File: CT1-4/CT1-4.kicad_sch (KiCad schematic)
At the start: 25 parts

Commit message: Some initial fixing of ERC errors.
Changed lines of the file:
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@@
 	)
 	(junction
-		(at 57.15 33.02)
-		(diameter 0)
-		(color 0 0 0 0)
-	)
-	(junction
 		(at 204.47 327.66)
 		(diameter 0)
@@
 	)
 	(junction
-		(at 119.38 119.38)
-		(diameter 0)
-		(color 0 0 0 0)
-	)
-	(junction
 		(at 476.25 129.54)
 		(diameter 0)
@@
 	(wire
 		(pts
-			(xy 57.15 29.21) (xy 57.15 33.02)
-		)
-		(stroke
-			(width 0)
-			(type default)
-		)
-	)
-	(wire
-		(pts
 			(xy 114.3 160.02) (xy 111.76 160.02)
 		)
@@
 	(wire
 		(pts
-			(xy 57.15 33.02) (xy 59.69 33.02)
+			(xy 48.26 33.02) (xy 59.69 33.02)
 		)
 		(stroke
@@
 	(wire
 		(pts
-			(xy 48.26 33.02) (xy 57.15 33.02)
-		)
-		(stroke
-			(width 0)
-			(type default)
-		)
-	)
-	(wire
-		(pts
 			(xy 341.63 287.02) (xy 350.52 287.02)
 		)
@@
 	(wire
 		(pts
-			(xy 119.38 118.11) (xy 119.38 119.38)
-		)
-		(stroke
-			(width 0)
-			(type default)
-		)
-	)
-	(wire
-		(pts
 			(xy 36.83 157.48) (xy 40.64 157.48)
 		)
@@
 	)
 	(symbol
-		(lib_id "power:PWR_FLAG")
-		(at 119.38 118.11 0)
-		(unit 1)
-		(body_style 1)
-		(exclude_from_sim no)
-		(in_bom yes)
-		(on_board yes)
-		(in_pos_files yes)
-		(dnp no)
-		(fields_autoplaced yes)
-		(property "Reference" "#FLG07"
-			(at 119.38 116.205 0)
-			(hide yes)
-			(show_name no)
-			(do_not_autoplace no)
-			(effects
-				(font
-					(size 1.27 1.27)
-				)
-			)
-		)
-		(property "Value" "PWR_FLAG"
-			(at 119.38 113.03 0)
-			(show_name no)
-			(do_not_autoplace no)
-			(effects
-				(font
-					(size 1.27 1.27)
-				)
-			)
-		)
-		(property "Footprint" ""
-			(at 119.38 118.11 0)
-			(hide yes)
-			(show_name no)
-			(do_not_autoplace no)
-			(effects
-				(font
-					(size 1.27 1.27)
-				)
-			)
-		)
-		(property "Datasheet" ""
-			(at 119.38 118.11 0)
-			(hide yes)
-			(show_name no)
-			(do_not_autoplace no)
-			(effects
-				(font
-					(size 1.27 1.27)
-				)
-			)
-		)
-		(property "Description" "Special symbol for telling ERC where power comes from"
-			(at 119.38 118.11 0)
-			(hide yes)
-			(show_name no)
-			(do_not_autoplace no)
-			(effects
-				(font
-					(size 1.27 1.27)
-				)
-			)
-		)
-		(pin "1"
-		)
-		(instances
-			(project "patinhofeio"
-				(path "/aca06203-542d-4682-a7e3-8839e24cce95/58050eef-51bb-485d-b6f6-c260fc96a7e7"
-					(reference "#FLG07")
-					(unit 1)
-				)
-			)
-		)
-	)
-	(symbol
 		(lib_id "power:GND")
 		(at 172.72 177.8 0)
@@
 					(unit 1)
 				)
-			)
-		)
-	)
-	(symbol
-		(lib_id "power:PWR_FLAG")
-		(at 57.15 29.21 0)
-		(unit 1)
-		(body_style 1)
-		(exclude_from_sim no)
-		(in_bom yes)
-		(on_board yes)
-		(in_pos_files yes)
-		(dnp no)
-		(fields_autoplaced yes)
-		(property "Reference" "#FLG057"
-			(at 57.15 27.305 0)
-			(hide yes)
-			(show_name no)
-			(do_not_autoplace no)
-			(effects
-				(font
-					(size 1.27 1.27)
-				)
-			)
-		)
-		(property "Value" "PWR_FLAG"
-			(at 57.15 24.13 0)
-			(show_name no)
-			(do_not_autoplace no)
-			(effects
-				(font
-					(size 1.27 1.27)
-				)
-			)
-		)
-		(property "Footprint" ""
-			(at 57.15 29.21 0)
-			(hide yes)
-			(show_name no)
-			(do_not_autoplace no)
-			(effects
-				(font
-					(size 1.27 1.27)
-				)
-			)
-		)
-		(property "Datasheet" ""
-			(at 57.15 29.21 0)
-			(hide yes)
-			(show_name no)
-			(do_not_autoplace no)
-			(effects
-				(font
-					(size 1.27 1.27)
-				)
-			)
-		)
-		(property "Description" "Special symbol for telling ERC where power comes from"
-			(at 57.15 29.21 0)
-			(hide yes)
-			(show_name no)
-			(do_not_autoplace no)
-			(effects
-				(font
-					(size 1.27 1.27)
-				)
-			)
-		)
-		(pin "1"
-		)
-		(instances
-			(project "patinhofeio"
-				(path "/aca06203-542d-4682-a7e3-8839e24cce95/58050eef-51bb-485d-b6f6-c260fc96a7e7"
-					(reference "#FLG057")
-					(unit 1)
-				)

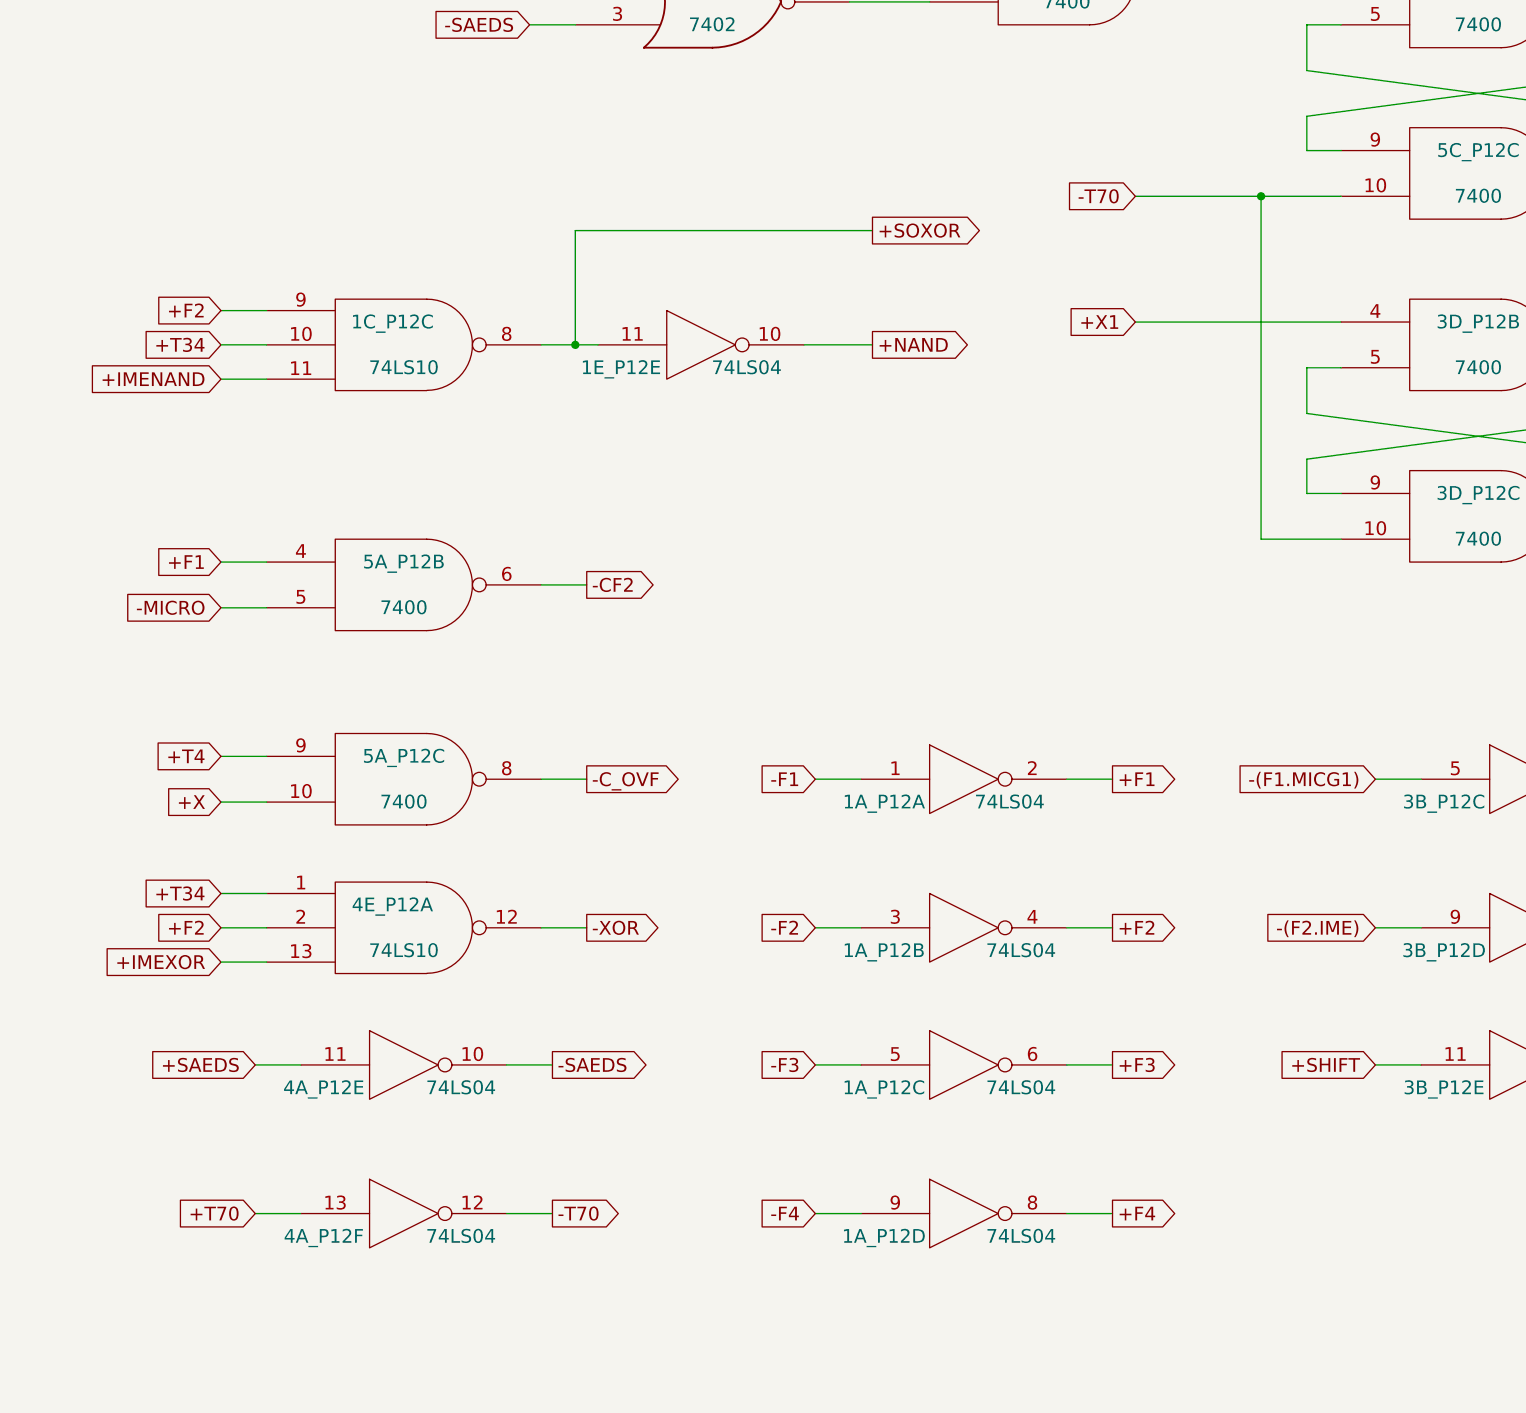
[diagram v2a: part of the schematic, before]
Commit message: addressing a few more ERC errors
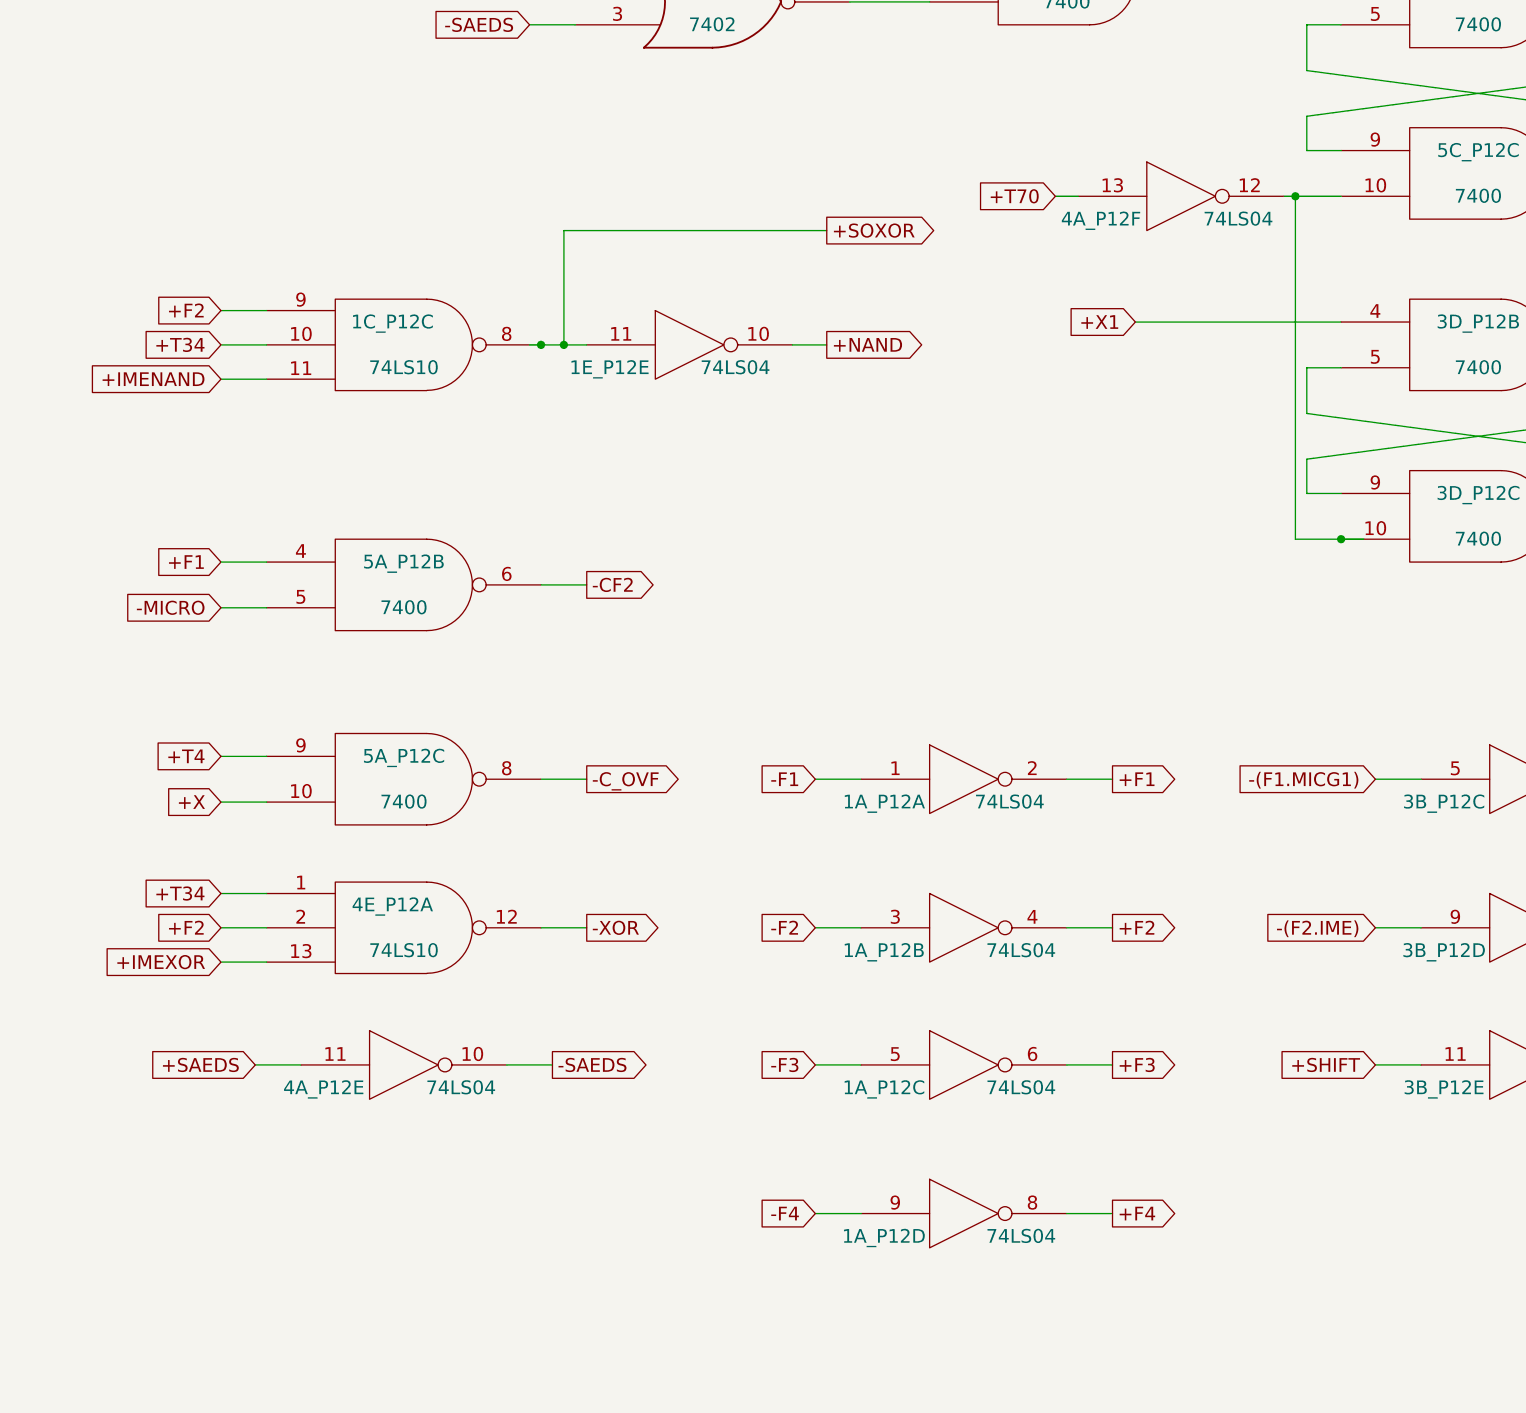
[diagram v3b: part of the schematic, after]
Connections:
- net -T70: no longer names the net of 3D_P12.10, 4A_P12.12, 5C_P12.10
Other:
- moved on the sheet: 1E_P12E, 4A_P12F
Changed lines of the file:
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@@
 	)
 	(junction
-		(at 422.91 132.08)
-		(diameter 0)
-		(color 0 0 0 0)
-	)
-	(junction
 		(at 476.25 147.32)
 		(diameter 0)
@@
 	)
 	(junction
+		(at 345.44 148.59)
+		(diameter 0)
+		(color 0 0 0 0)
+	)
+	(junction
 		(at 111.76 171.45)
 		(diameter 0)
@@
 	)
 	(junction
+		(at 342.9 148.59)
+		(diameter 0)
+		(color 0 0 0 0)
+	)
+	(junction
 		(at 466.09 148.59)
 		(diameter 0)
@@
 	)
 	(junction
+		(at 431.8 170.18)
+		(diameter 0)
+		(color 0 0 0 0)
+	)
+	(junction
 		(at 476.25 111.76)
 		(diameter 0)
@@
 	)
 	(junction
-		(at 346.71 148.59)
+		(at 158.75 354.33)
 		(diameter 0)
 		(color 0 0 0 0)
 	)
 	(junction
-		(at 158.75 354.33)
+		(at 426.72 132.08)
 		(diameter 0)
 		(color 0 0 0 0)
@@
 	(wire
 		(pts
-			(xy 346.71 135.89) (xy 346.71 148.59)
+			(xy 345.44 135.89) (xy 345.44 148.59)
 		)
 		(stroke
@@
 	(wire
 		(pts
-			(xy 316.23 245.11) (xy 311.15 245.11)
+			(xy 402.59 132.08) (xy 400.05 132.08)
 		)
 		(stroke
@@
 	(wire
 		(pts
-			(xy 422.91 170.18) (xy 431.8 170.18)
+			(xy 426.72 170.18) (xy 431.8 170.18)
 		)
 		(stroke
@@
 	(wire
 		(pts
+			(xy 426.72 132.08) (xy 425.45 132.08)
+		)
+		(stroke
+			(width 0)
+			(type default)
+		)
+	)
+	(wire
+		(pts
 			(xy 365.76 34.29) (xy 397.51 34.29)
 		)
@@
 	(wire
 		(pts
-			(xy 422.91 132.08) (xy 422.91 170.18)
+			(xy 426.72 132.08) (xy 426.72 170.18)
 		)
 		(stroke
@@
 	(wire
 		(pts
+			(xy 434.34 170.18) (xy 431.8 170.18)
+		)
+		(stroke
+			(width 0)
+			(type default)
+		)
+	)
+	(wire
+		(pts
 			(xy 36.83 119.38) (xy 59.69 119.38)
 		)
@@
 	(wire
 		(pts
-			(xy 344.17 245.11) (xy 339.09 245.11)
+			(xy 431.8 107.95) (xy 416.56 107.95)
 		)
 		(stroke
@@
 	(wire
 		(pts
-			(xy 431.8 107.95) (xy 416.56 107.95)
+			(xy 509.27 287.02) (xy 514.35 287.02)
 		)
 		(stroke
@@
 	(wire
 		(pts
-			(xy 509.27 287.02) (xy 514.35 287.02)
+			(xy 370.84 148.59) (xy 374.65 148.59)
 		)
 		(stroke
@@
 	(wire
 		(pts
-			(xy 372.11 148.59) (xy 379.73 148.59)
+			(xy 342.9 148.59) (xy 345.44 148.59)
 		)
 		(stroke
@@
 	(wire
 		(pts
-			(xy 379.73 135.89) (xy 346.71 135.89)
+			(xy 374.65 135.89) (xy 345.44 135.89)
 		)
 		(stroke
@@
 	(wire
 		(pts
-			(xy 346.71 148.59) (xy 349.25 148.59)
-		)
-		(stroke
-			(width 0)
-			(type default)
-		)
-	)
-	(wire
-		(pts
-			(xy 408.94 132.08) (xy 422.91 132.08)
+			(xy 345.44 148.59) (xy 347.98 148.59)
 		)
 		(stroke
@@
 	(wire
 		(pts
-			(xy 342.9 148.59) (xy 346.71 148.59)
-		)
-		(stroke
-			(width 0)
-			(type default)
-		)
-	)
-	(wire
-		(pts
-			(xy 422.91 132.08) (xy 431.8 132.08)
+			(xy 341.63 148.59) (xy 342.9 148.59)
 		)
 		(stroke
@@
 	(wire
 		(pts
+			(xy 426.72 132.08) (xy 431.8 132.08)
+		)
+		(stroke
+			(width 0)
+			(type default)
+		)
+	)
+	(wire
+		(pts
 			(xy 394.97 292.1) (xy 389.89 292.1)
 		)
@@
 		)
 	)
-	(global_label "-T70"
-		(shape input)
-		(at 408.94 132.08 180)
-		(effects
-			(font
-				(size 1.524 1.524)
-			)
-			(justify right)
-		)
-		(property "Intersheetrefs" "${INTERSHEET_REFS}"
-			(at 408.94 132.08 0)
-			(hide yes)
-			(show_name no)
-			(do_not_autoplace no)
-			(effects
-				(font
-					(size 1.27 1.27)
-				)
-			)
-		)
-	)
 	(global_label "+RD_7"
 		(shape output)
@@
 	(global_label "+T70"
 		(shape input)
-		(at 311.15 245.11 180)
+		(at 400.05 132.08 180)
 		(effects
 			(font
@@
 		)
 		(property "Intersheetrefs" "${INTERSHEET_REFS}"
-			(at 311.15 245.11 0)
+			(at 400.05 132.08 0)
 			(hide yes)
 			(show_name no)
@@
 	(global_label "+SOXOR"
 		(shape output)
-		(at 379.73 135.89 0)
+		(at 374.65 135.89 0)
 		(effects
 			(font
@@
 		)
 		(property "Intersheetrefs" "${INTERSHEET_REFS}"
-			(at 379.73 135.89 0)
+			(at 374.65 135.89 0)
 			(hide yes)
 			(show_name no)
@@
 		)
 	)
-	(global_label "-T70"
-		(shape output)
-		(at 344.17 245.11 0)
-		(effects
-			(font
-				(size 1.524 1.524)
-			)
-			(justify left)
-		)
-		(property "Intersheetrefs" "${INTERSHEET_REFS}"
-			(at 344.17 245.11 0)
-			(hide yes)
-			(show_name no)
-			(do_not_autoplace no)
-			(effects
-				(font
-					(size 1.27 1.27)
-				)
-			)
-		)
-	)
 	(global_label "-(F3.SOM)"
 		(shape input)
@@
 	(global_label "+NAND"
 		(shape output)
-		(at 379.73 148.59 0)
+		(at 374.65 148.59 0)
 		(effects
 			(font
@@
 		)
 		(property "Intersheetrefs" "${INTERSHEET_REFS}"
-			(at 379.73 148.59 0)
+			(at 374.65 148.59 0)
 			(hide yes)
 			(show_name no)
@@
 	(symbol
 		(lib_id "CT1-4-rescue:74LS04")
-		(at 327.66 245.11 0)
+		(at 414.02 132.08 0)
 		(unit 6)
 		(body_style 1)
@@
 		(dnp no)
 		(property "Reference" "4A_P12"
-			(at 318.77 247.65 0)
+			(at 405.13 134.62 0)
 			(show_name no)
 			(do_not_autoplace no)
@@
 		)
 		(property "Value" "74LS04"
-			(at 334.01 247.65 0)
+			(at 420.37 134.62 0)
 			(show_name no)
 			(do_not_autoplace no)
@@
 		)
 		(property "Footprint" ""
-			(at 327.66 245.11 0)
+			(at 414.02 132.08 0)
 			(show_name no)
 			(do_not_autoplace no)
@@
 		)
 		(property "Datasheet" ""
-			(at 327.66 245.11 0)
+			(at 414.02 132.08 0)
 			(show_name no)
 			(do_not_autoplace no)
@@
 		)
 		(property "Description" ""
-			(at 327.66 245.11 0)
+			(at 414.02 132.08 0)
 			(show_name no)
 			(do_not_autoplace no)
@@
 	(symbol
 		(lib_id "CT1-4-rescue:74LS04")
-		(at 360.68 148.59 0)
+		(at 359.41 148.59 0)
 		(unit 5)
 		(body_style 1)
@@
 		(dnp no)
 		(property "Reference" "1E_P12"
-			(at 351.79 151.13 0)
+			(at 350.52 151.13 0)
 			(show_name no)
 			(do_not_autoplace no)
@@
 		)
 		(property "Value" "74LS04"
-			(at 365.76 151.13 0)
+			(at 364.49 151.13 0)
 			(show_name no)
 			(do_not_autoplace no)
@@
 		)
 		(property "Footprint" ""
-			(at 360.68 148.59 0)
+			(at 359.41 148.59 0)
 			(show_name no)
 			(do_not_autoplace no)
@@
 		)
 		(property "Datasheet" ""
-			(at 360.68 148.59 0)
+			(at 359.41 148.59 0)
 			(show_name no)
 			(do_not_autoplace no)
@@
 		)
 		(property "Description" ""
-			(at 360.68 148.59 0)
+			(at 359.41 148.59 0)
 			(show_name no)
 			(do_not_autoplace no)

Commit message: fixing a whole bunch more ERC errors
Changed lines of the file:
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@@
+		)
+	)
+	(label "-RI_6"
+		(at 316.23 378.46 180)
+		(effects
+			(font
+				(size 1.524 1.524)
+			)
+			(justify right bottom)
+		)
+	)
+	(label "-RI_6"
+		(at 530.86 242.57 0)
+		(effects
+			(font
+				(size 1.524 1.524)
+			)
+			(justify left bottom)
 		)
 	)
@@
 		)
 	)
-	(global_label "-RI_6"
-		(shape output)
-		(at 530.86 242.57 0)
-		(effects
-			(font
-				(size 1.524 1.524)
-			)
-			(justify left)
-		)
-		(property "Intersheetrefs" "${INTERSHEET_REFS}"
-			(at 530.86 242.57 0)
-			(hide yes)
-			(show_name no)
-			(do_not_autoplace no)
-			(effects
-				(font
-					(size 1.27 1.27)
-				)
-			)
-		)
-	)
 	(global_label "-SAEDS"
 		(shape input)
@@
 			(hide yes)
 			(show_name no)
-			(do_not_autoplace no)
-			(effects
-				(font
-					(size 1.27 1.27)
-				)
-			)
-		)
-	)
-	(global_label "-RI_6"
-		(shape input)
-		(at 316.23 378.46 180)
-		(effects
-			(font
-				(size 1.524 1.524)
-			)
-			(justify right)
-		)
-		(property "Intersheetrefs" "${INTERSHEET_REFS}"
-			(at 316.23 378.46 0)
-			(hide yes)
-			(show_name no)

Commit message: a lot more work on the circuit transcription
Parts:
- removed 1A_P12, 4A_P12: 74LS04, symbol CT1-4-rescue:74LS04
- removed unit 3 of 2B_P12
- removed unit 1 of 2B_P12
- removed unit 2 of 2B_P12
- removed unit 5 of 3B_P12
- removed unit 4 of 3B_P12
- removed unit 3 of 3B_P12
- removed unit 1 of 3B_P12
- removed 5B_P12: 7402, symbol CT1-4-rescue:7402
- added 1A_P12, 4A_P12: 74LS04, symbol 74xx:74LS04
- added unit 1 of 2B_P12
- added unit 2 of 2B_P12
- added unit 5 of 2B_P12
- added unit 3 of 2B_P12
- added unit 3 of 3B_P12
- added unit 5 of 3B_P12
- added unit 6 of 3B_P12
- added unit 1 of 3B_P12
- added unit 4 of 3B_P12
- added unit 7 of 3B_P12
- added 5B_P12: 7402, symbol 74xx:7402
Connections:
- net +(F1.MICG1): now also 3B_P12.6
- net +(F2.IME): now also 3B_P12.8
- net +(F2.SAEDE): now also 2B_P12.4
- net +F1: now also 1A_P12.2
- net +F2: now also 1A_P12.4
- net +F3: now also 1A_P12.6
- net +F4: now also 1A_P12.8
- net +MICRO: now also 4A_P12.5
- net +RI_6: now also 4A_P12.9
- net +SAEDE: now also 4A_P12.3
- net +SAEDS: now also 4A_P12.11
- net +SHIFT: now also 3B_P12.11
- net +T70: now also 4A_P12.13
- net +TRI: now also 2B_P12.9
- net +TRO: now also 2B_P12.8
- net +X: now also 4A_P12.1
- net +Z: now also 3B_P12.2
- net -(F1.MICG1): now also 3B_P12.5
- net -(F2.IME): now also 3B_P12.9
- net -F1: now also 1A_P12.1
- net -F2: now also 1A_P12.3, 2B_P12.3, 2B_P12.5, 5B_P12.2
- net -F3: now also 1A_P12.5
- net -F4: now also 1A_P12.9
- net -MICRO: now also 4A_P12.6
- net -RI_6: now also 4A_P12.8
- net -SAEDE: now also 2B_P12.6, 4A_P12.4
- net -SAEDS: now also 4A_P12.10, 5B_P12.3
- net -SHIFT: now also 2B_P12.2, 3B_P12.10
- net -X: now also 4A_P12.2
- net -Y: now also 1A_P12.12
- net GND: now also 1A_P12.7 (GND), 2B_P12.7 (GND), 3B_P12.7 (GND), 4A_P12.7 (GND), 5B_P12.7 (GND)
- net P12_3A6: now also 5B_P12.11, 5B_P12.12
- net VCC: now also 1A_P12.14 (VCC), 2B_P12.14 (VCC), 3B_P12.14 (VCC), 4A_P12.14 (VCC), 5B_P12.14 (VCC)
- net at 3D_P12.10, 5C_P12.10: now also 4A_P12.12
- net at 1B_P12.4: now also 1A_P12.10
- net at 1C_P12.12: now also 1A_P12.13
- net at 5C_P12.2: now also 5B_P12.1
- net at 1D_P12.9: now also 5B_P12.13
- net at 3A_P12.12: now also 3B_P12.1
- net at 2D_P12.13, 2D_P12.8, 2E_P12.13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: now also 2B_P12.1
- new net: 1A_P12.11, 2B_P12.10
- no-connect marks 17 -> 21
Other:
- moved on the sheet: 4C_P12C, 4C_P12D
